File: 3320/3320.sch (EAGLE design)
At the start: 69 parts, among them IC1 OPA2134P, IC2 OPA2134P, X1 2516-

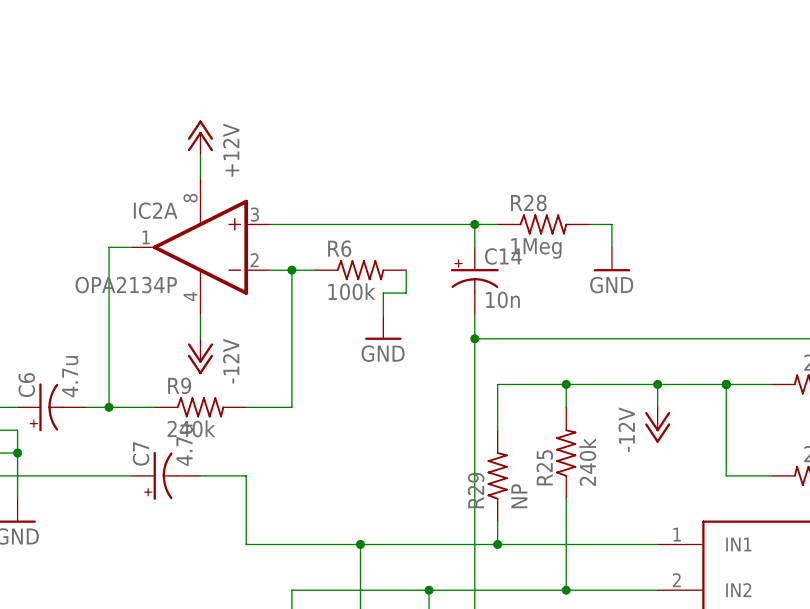
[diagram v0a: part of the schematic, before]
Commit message: fixed the 2 pole polarity for 3320
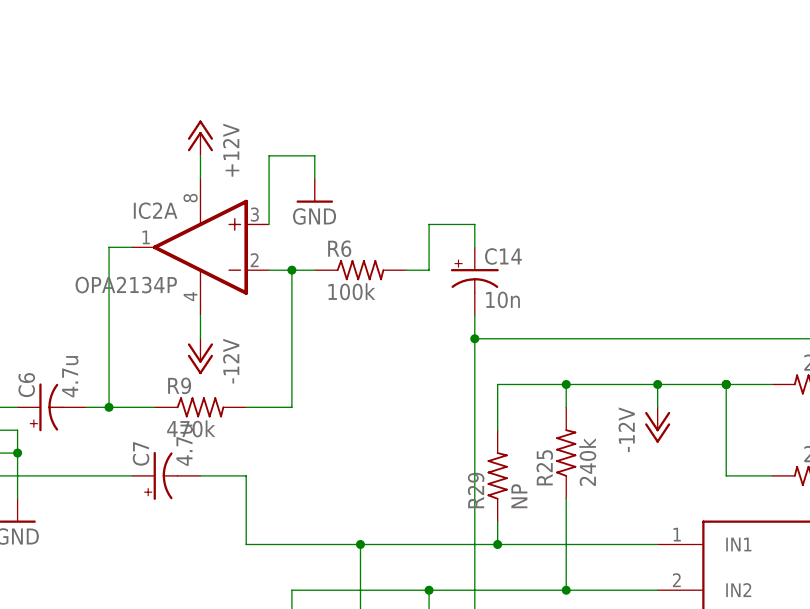
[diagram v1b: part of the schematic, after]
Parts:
- removed R28: 1Meg, dan:R-US_0207/2V
- R9: value 240k -> 470k
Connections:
- net GND: now also IC2A.+IN; no longer R28.2, R6.2
- net N$11: now also R6.2; no longer IC2A.+IN, R28.1
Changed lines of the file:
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@@
 <part name="P+9" library="dan" deviceset="+12V" device=""/>
 <part name="P-8" library="dan" deviceset="-12V" device=""/>
-<part name="R9" library="dan" deviceset="R-US_" device="0207/2V" value="240k"/>
+<part name="R9" library="dan" deviceset="R-US_" device="0207/2V" value="470k"/>
 <part name="GND22" library="dan" deviceset="GND" device=""/>
 <part name="R13" library="dan" deviceset="R-US_" device="0207/2V" value="100k"/>
@@
 <part name="R27" library="dan" deviceset="R-US_" device="0207/2V" value="240k"/>
 <part name="C14" library="dan" deviceset="CPOL-US" device="E2.5-6" value="10n"/>
-<part name="R28" library="dan" deviceset="R-US_" device="0207/2V" value="1Meg"/>
-<part name="GND27" library="dan" deviceset="GND" device=""/>
 <part name="C15" library="dan" deviceset="CPOL-US" device="E2.5-6" value="2.2u"/>
 <part name="C16" library="dan" deviceset="CPOL-US" device="E2.5-6" value="2.2u"/>
@@
 <instance part="P-8" gate="1" x="20.32" y="81.28" rot="MR0"/>
 <instance part="R9" gate="G$1" x="20.32" y="76.2"/>
-<instance part="GND22" gate="1" x="40.64" y="83.82"/>
+<instance part="GND22" gate="1" x="33.02" y="99.06"/>
 <instance part="R13" gate="G$1" x="43.18" y="-17.78"/>
 <instance part="GND23" gate="1" x="50.8" y="-22.86"/>
@@
 <instance part="R27" gate="G$1" x="88.9" y="78.74" rot="R180"/>
 <instance part="C14" gate="G$1" x="50.8" y="91.44"/>
-<instance part="R28" gate="G$1" x="58.42" y="96.52"/>
-<instance part="GND27" gate="1" x="66.04" y="91.44"/>
 <instance part="C15" gate="G$1" x="241.3" y="25.4"/>
 <instance part="C16" gate="G$1" x="241.3" y="12.7"/>
@@
 <junction x="218.44" y="68.58"/>
 <junction x="218.44" y="71.12"/>
-</segment>
-<segment>
-<pinref part="GND22" gate="1" pin="GND"/>
-<wire x1="40.64" y1="86.36" x2="40.64" y2="88.9" width="0.1524" layer="91"/>
-<wire x1="40.64" y1="88.9" x2="43.18" y2="88.9" width="0.1524" layer="91"/>
-<pinref part="R6" gate="G$1" pin="2"/>
-<wire x1="43.18" y1="88.9" x2="43.18" y2="91.44" width="0.1524" layer="91"/>
 </segment>
 <segment>
@@
 </segment>
 <segment>
-<pinref part="GND27" gate="1" pin="GND"/>
-<wire x1="66.04" y1="93.98" x2="66.04" y2="96.52" width="0.1524" layer="91"/>
-<pinref part="R28" gate="G$1" pin="2"/>
-<wire x1="66.04" y1="96.52" x2="63.5" y2="96.52" width="0.1524" layer="91"/>
-</segment>
-<segment>
 <pinref part="Q" gate="G$1" pin="A"/>
 <wire x1="226.06" y1="73.66" x2="226.06" y2="78.74" width="0.1524" layer="91"/>
@@
 <pinref part="GND6" gate="1" pin="GND"/>
 <wire x1="231.14" y1="78.74" x2="231.14" y2="76.2" width="0.1524" layer="91"/>
+</segment>
+<segment>
+<pinref part="IC2" gate="A" pin="+IN"/>
+<wire x1="27.94" y1="96.52" x2="27.94" y2="104.14" width="0.1524" layer="91"/>
+<pinref part="GND22" gate="1" pin="GND"/>
+<wire x1="27.94" y1="104.14" x2="33.02" y2="104.14" width="0.1524" layer="91"/>
+<wire x1="33.02" y1="104.14" x2="33.02" y2="101.6" width="0.1524" layer="91"/>
 </segment>
 </net>
@@
 <net name="N$11" class="0">
 <segment>
-<pinref part="IC2" gate="A" pin="+IN"/>
-<wire x1="27.94" y1="96.52" x2="50.8" y2="96.52" width="0.1524" layer="91"/>
 <pinref part="C14" gate="G$1" pin="+"/>
-<pinref part="R28" gate="G$1" pin="1"/>
-<wire x1="53.34" y1="96.52" x2="50.8" y2="96.52" width="0.1524" layer="91"/>
 <wire x1="50.8" y1="96.52" x2="50.8" y2="93.98" width="0.1524" layer="91"/>
-<junction x="50.8" y="96.52"/>
+<pinref part="R6" gate="G$1" pin="2"/>
+<wire x1="43.18" y1="91.44" x2="45.72" y2="91.44" width="0.1524" layer="91"/>
+<wire x1="45.72" y1="91.44" x2="45.72" y2="96.52" width="0.1524" layer="91"/>
+<wire x1="45.72" y1="96.52" x2="50.8" y2="96.52" width="0.1524" layer="91"/>
 </segment>
 </net>

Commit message: fixed footprints on top 3320 board
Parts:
- R14, R15, R7, R8: device dan:R-US_0309/12 -> dan:R-US_0204/7
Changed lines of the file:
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@@
 <grid distance="0.1" unitdist="inch" unit="inch" style="lines" multiple="1" display="no" altdistance="0.01" altunitdist="inch" altunit="inch"/>
 <layers>
-<layer number="1" name="Top" color="4" fill="1" visible="no" active="no"/>
-<layer number="2" name="Route2" color="1" fill="3" visible="no" active="no"/>
-<layer number="3" name="Route3" color="4" fill="3" visible="no" active="no"/>
-<layer number="4" name="Route4" color="1" fill="4" visible="no" active="no"/>
-<layer number="5" name="Route5" color="4" fill="4" visible="no" active="no"/>
-<layer number="6" name="Route6" color="1" fill="8" visible="no" active="no"/>
-<layer number="7" name="Route7" color="4" fill="8" visible="no" active="no"/>
-<layer number="8" name="Route8" color="1" fill="2" visible="no" active="no"/>
-<layer number="9" name="Route9" color="4" fill="2" visible="no" active="no"/>
-<layer number="10" name="Route10" color="1" fill="7" visible="no" active="no"/>
-<layer number="11" name="Route11" color="4" fill="7" visible="no" active="no"/>
-<layer number="12" name="Route12" color="1" fill="5" visible="no" active="no"/>
-<layer number="13" name="Route13" color="4" fill="5" visible="no" active="no"/>
-<layer number="14" name="Route14" color="1" fill="6" visible="no" active="no"/>
-<layer number="15" name="Route15" color="4" fill="6" visible="no" active="no"/>
-<layer number="16" name="Bottom" color="1" fill="1" visible="no" active="no"/>
-<layer number="17" name="Pads" color="2" fill="1" visible="no" active="no"/>
-<layer number="18" name="Vias" color="2" fill="1" visible="no" active="no"/>
-<layer number="19" name="Unrouted" color="6" fill="1" visible="no" active="no"/>
-<layer number="20" name="Dimension" color="15" fill="1" visible="no" active="no"/>
-<layer number="21" name="tPlace" color="7" fill="1" visible="no" active="no"/>
-<layer number="22" name="bPlace" color="7" fill="1" visible="no" active="no"/>
-<layer number="23" name="tOrigins" color="15" fill="1" visible="no" active="no"/>
-<layer number="24" name="bOrigins" color="15" fill="1" visible="no" active="no"/>
-<layer number="25" name="tNames" color="7" fill="1" visible="no" active="no"/>
-<layer number="26" name="bNames" color="7" fill="1" visible="no" active="no"/>
-<layer number="27" name="tValues" color="7" fill="1" visible="no" active="no"/>
-<layer number="28" name="bValues" color="7" fill="1" visible="no" active="no"/>
+<layer number="1" name="Top" color="4" fill="1" visible="yes" active="no"/>
+<layer number="2" name="Route2" color="1" fill="3" visible="yes" active="no"/>
+<layer number="3" name="Route3" color="4" fill="3" visible="yes" active="no"/>
+<layer number="4" name="Route4" color="1" fill="4" visible="yes" active="no"/>
+<layer number="5" name="Route5" color="4" fill="4" visible="yes" active="no"/>
+<layer number="6" name="Route6" color="1" fill="8" visible="yes" active="no"/>
+<layer number="7" name="Route7" color="4" fill="8" visible="yes" active="no"/>
+<layer number="8" name="Route8" color="1" fill="2" visible="yes" active="no"/>
+<layer number="9" name="Route9" color="4" fill="2" visible="yes" active="no"/>
+<layer number="10" name="Route10" color="1" fill="7" visible="yes" active="no"/>
+<layer number="11" name="Route11" color="4" fill="7" visible="yes" active="no"/>
+<layer number="12" name="Route12" color="1" fill="5" visible="yes" active="no"/>
+<layer number="13" name="Route13" color="4" fill="5" visible="yes" active="no"/>
+<layer number="14" name="Route14" color="1" fill="6" visible="yes" active="no"/>
+<layer number="15" name="Route15" color="4" fill="6" visible="yes" active="no"/>
+<layer number="16" name="Bottom" color="1" fill="1" visible="yes" active="no"/>
+<layer number="17" name="Pads" color="2" fill="1" visible="yes" active="no"/>
+<layer number="18" name="Vias" color="2" fill="1" visible="yes" active="no"/>
+<layer number="19" name="Unrouted" color="6" fill="1" visible="yes" active="no"/>
+<layer number="20" name="Dimension" color="15" fill="1" visible="yes" active="no"/>
+<layer number="21" name="tPlace" color="7" fill="1" visible="yes" active="no"/>
+<layer number="22" name="bPlace" color="7" fill="1" visible="yes" active="no"/>
+<layer number="23" name="tOrigins" color="15" fill="1" visible="yes" active="no"/>
+<layer number="24" name="bOrigins" color="15" fill="1" visible="yes" active="no"/>
+<layer number="25" name="tNames" color="7" fill="1" visible="yes" active="no"/>
+<layer number="26" name="bNames" color="7" fill="1" visible="yes" active="no"/>
+<layer number="27" name="tValues" color="7" fill="1" visible="yes" active="no"/>
+<layer number="28" name="bValues" color="7" fill="1" visible="yes" active="no"/>
 <layer number="29" name="tStop" color="7" fill="3" visible="no" active="no"/>
 <layer number="30" name="bStop" color="7" fill="6" visible="no" active="no"/>
@@
 <layer number="35" name="tGlue" color="7" fill="4" visible="no" active="no"/>
 <layer number="36" name="bGlue" color="7" fill="5" visible="no" active="no"/>
-<layer number="37" name="tTest" color="7" fill="1" visible="no" active="no"/>
-<layer number="38" name="bTest" color="7" fill="1" visible="no" active="no"/>
+<layer number="37" name="tTest" color="7" fill="1" visible="yes" active="no"/>
+<layer number="38" name="bTest" color="7" fill="1" visible="yes" active="no"/>
 <layer number="39" name="tKeepout" color="4" fill="11" visible="no" active="no"/>
 <layer number="40" name="bKeepout" color="1" fill="11" visible="no" active="no"/>
@@
 <layer number="44" name="Drills" color="7" fill="1" visible="no" active="no"/>
 <layer number="45" name="Holes" color="7" fill="1" visible="no" active="no"/>
-<layer number="46" name="Milling" color="3" fill="1" visible="no" active="no"/>
-<layer number="47" name="Measures" color="7" fill="1" visible="no" active="no"/>
-<layer number="48" name="Document" color="7" fill="1" visible="no" active="no"/>
-<layer number="49" name="Reference" color="7" fill="1" visible="no" active="no"/>
-<layer number="51" name="tDocu" color="7" fill="1" visible="no" active="no"/>
-<layer number="52" name="bDocu" color="7" fill="1" visible="no" active="no"/>
+<layer number="46" name="Milling" color="3" fill="1" visible="yes" active="no"/>
+<layer number="47" name="Measures" color="7" fill="1" visible="yes" active="no"/>
+<layer number="48" name="Document" color="7" fill="1" visible="yes" active="no"/>
+<layer number="49" name="Reference" color="7" fill="1" visible="yes" active="no"/>
+<layer number="51" name="tDocu" color="7" fill="1" visible="yes" active="no"/>
+<layer number="52" name="bDocu" color="7" fill="1" visible="yes" active="no"/>
 <layer number="90" name="Modules" color="5" fill="1" visible="yes" active="yes"/>
 <layer number="91" name="Nets" color="2" fill="1" visible="yes" active="yes"/>
@@
 <part name="GND5" library="dan" deviceset="GND" device=""/>
 <part name="FC" library="dan" deviceset="US-EVU" device="F2J"/>
-<part name="R14" library="dan" deviceset="R-US_" device="0309/12" value="short"/>
-<part name="R15" library="dan" deviceset="R-US_" device="0309/12" value="10k"/>
+<part name="R14" library="dan" deviceset="R-US_" device="0204/7" value="short"/>
+<part name="R15" library="dan" deviceset="R-US_" device="0204/7" value="10k"/>
 <part name="P+3" library="dan" deviceset="+12V" device=""/>
 <part name="P-3" library="dan" deviceset="-12V" device=""/>
@@
 <part name="IN2" library="dan" deviceset="PJ301BM" device=""/>
 <part name="GND4" library="dan" deviceset="GND" device=""/>
-<part name="R7" library="dan" deviceset="R-US_" device="0309/12" value="100k"/>
-<part name="R8" library="dan" deviceset="R-US_" device="0309/12" value="100k"/>
+<part name="R7" library="dan" deviceset="R-US_" device="0204/7" value="100k"/>
+<part name="R8" library="dan" deviceset="R-US_" device="0204/7" value="100k"/>
 <part name="GND20" library="dan" deviceset="GND" device=""/>
 <part name="GND21" library="dan" deviceset="GND" device=""/>

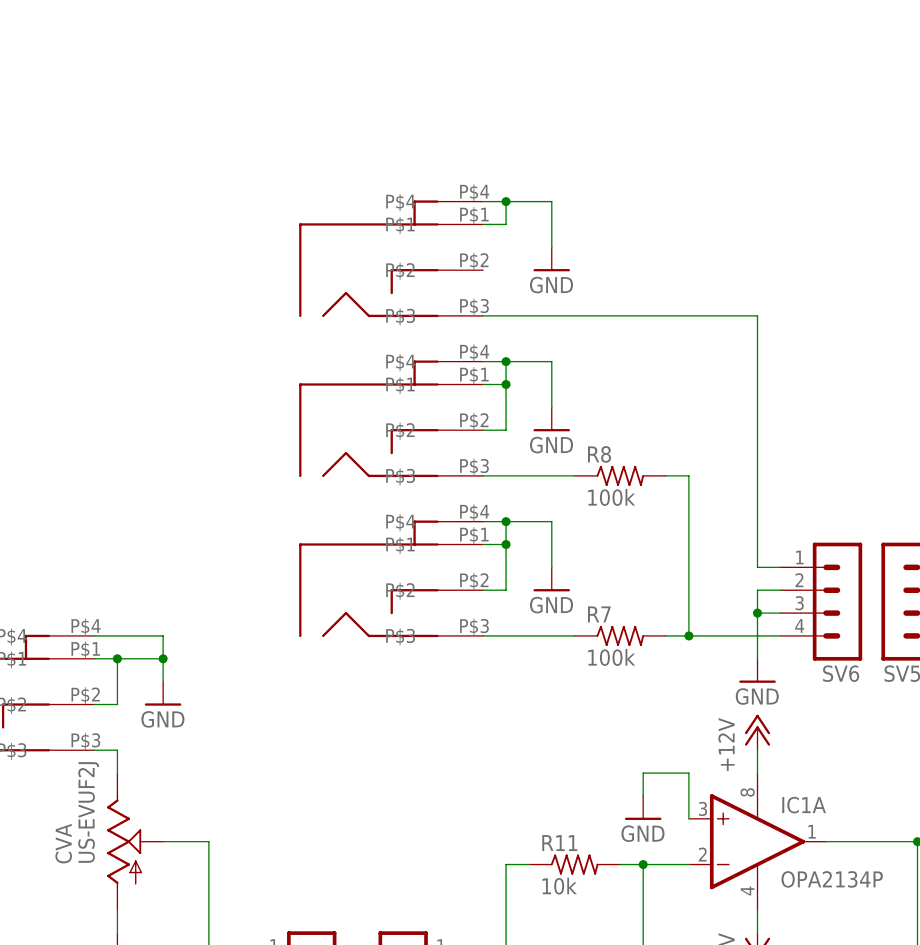
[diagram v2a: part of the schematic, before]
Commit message: added input atten pots to 3320 and re arranged front
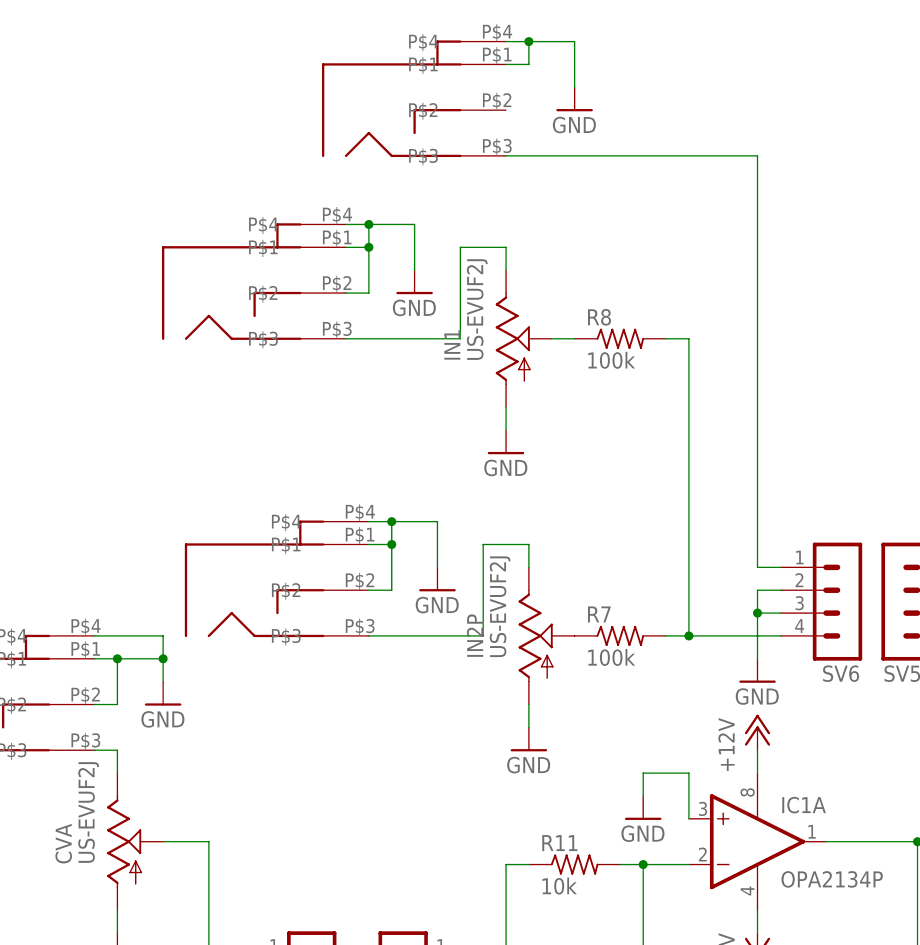
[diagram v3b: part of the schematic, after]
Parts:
- added IN1, IN2P: US-EVUF2J, dan:US-EVUF2J
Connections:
- new net N$44: IN.P$3, IN1.E
- new net N$46: IN2.P$3, IN2P.E
- net GND: now also IN1.A, IN2P.A
- net N$15: now also IN1.S; no longer IN.P$3
- net N$29: now also IN2P.S; no longer IN2.P$3
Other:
- moved on the sheet: R8
